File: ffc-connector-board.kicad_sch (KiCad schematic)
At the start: 8 parts, among them J1 1-84953-0, J2 Conn_01x10_Male, J3 Conn_01x10_Male, J4 200485-0710, J5 200528-0100, J6 Conn_01x10_Male, J7 505110-1092, J8 Conn_01x10_Male

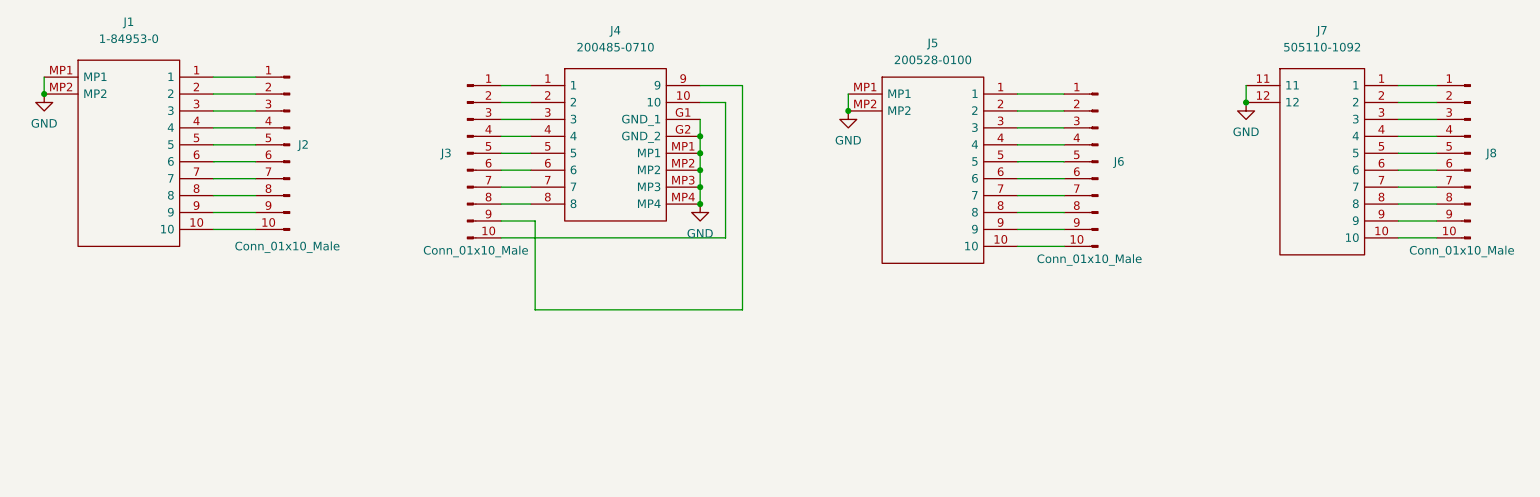
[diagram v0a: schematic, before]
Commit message: 2nd version with smaller connectors
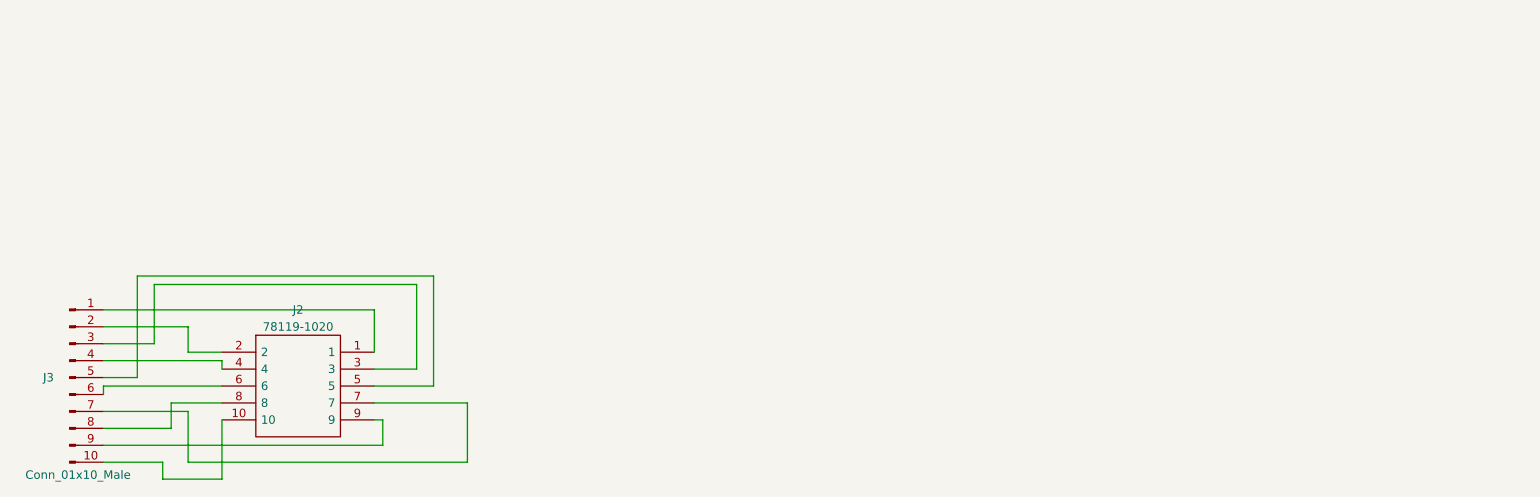
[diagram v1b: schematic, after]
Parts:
- removed J1: 1-84953-0, 1849530, symbol ffc-connectors:1-84953-0
- removed J2, J6, J8: Conn_01x10_Male, symbol Connector:Conn_01x10_Male
- removed J4: 200485-0710, 2004850710, symbol ffc-connectors:200485-0710
- removed J5: 200528-0100, 2005280100, symbol ffc-connectors:200528-0100
- removed J7: 505110-1092, 5051101092, symbol ffc-connectors:505110-1092
- added J2: 78119-1020, SamacSys_Parts:781191020, symbol SamacSys_Parts:78119-1020
- J3: footprint (none) -> Connector_PinHeader_2.54mm:PinHeader_1x10_P2.54mm_Vertical
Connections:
- net at J3.1 (Pin_1): now also J2.1
- net at J3.10 (Pin_10): now also J2.10
- net at J3.2 (Pin_2): now also J2.2
- net at J3.3 (Pin_3): now also J2.3
- net at J3.4 (Pin_4): now also J2.4
- net at J3.5 (Pin_5): now also J2.5
- net at J3.6 (Pin_6): now also J2.6
- net at J3.7 (Pin_7): now also J2.7
- net at J3.8 (Pin_8): now also J2.8
- net at J3.9 (Pin_9): now also J2.9
